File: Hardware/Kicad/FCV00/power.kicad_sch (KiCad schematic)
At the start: 52 parts, among them U1 TPS54360BDDAR, U2 TPS54360BDDAR, U3 AP2112K-3.3TRG1, U4 AP2112K-3.3TRG1

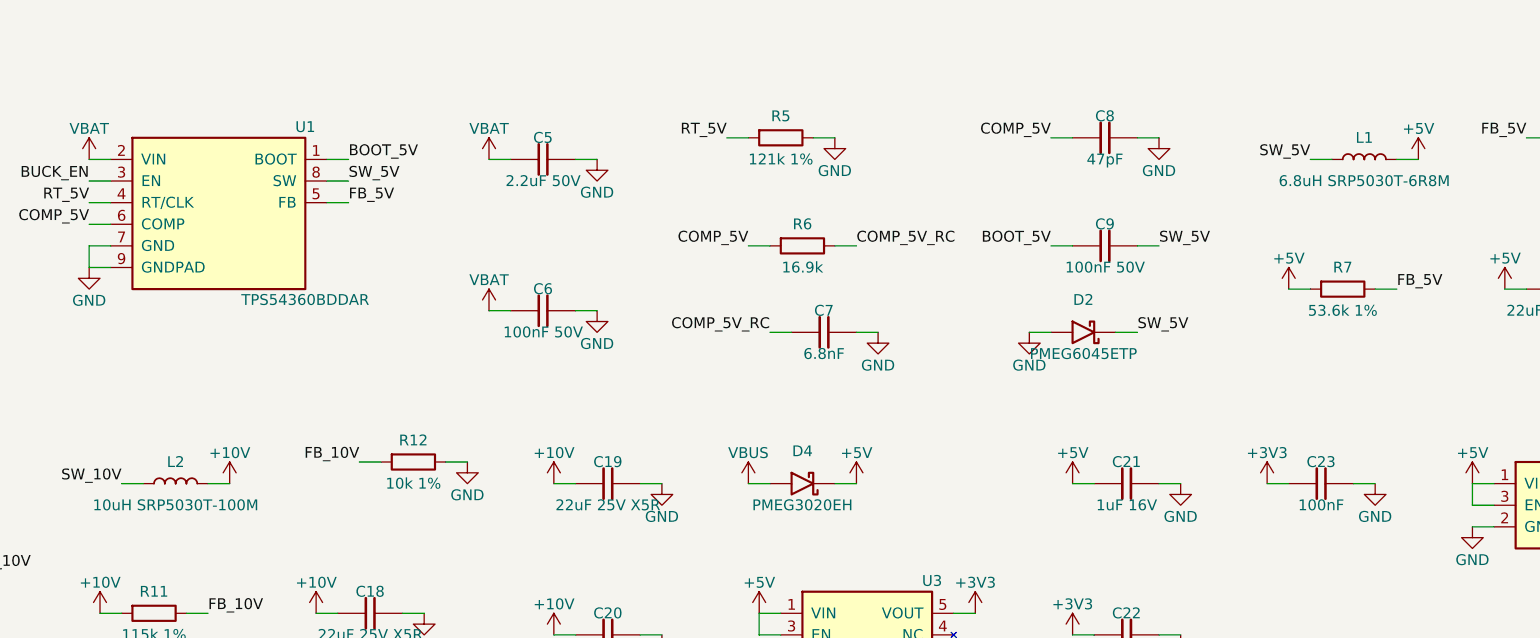
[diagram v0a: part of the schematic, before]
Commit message: Upgrade to KiCad 10 and use shared Kicad_Libs only
- Upgrade ESCV00, FCV00, RXV00, VTXV00 schematics and PCBs to KiCad 10
- Remove KiCad_Libs_Drone and merge_libs (parts already in Kicad_Libs)
- Lib tables list every Kicad_Libs library
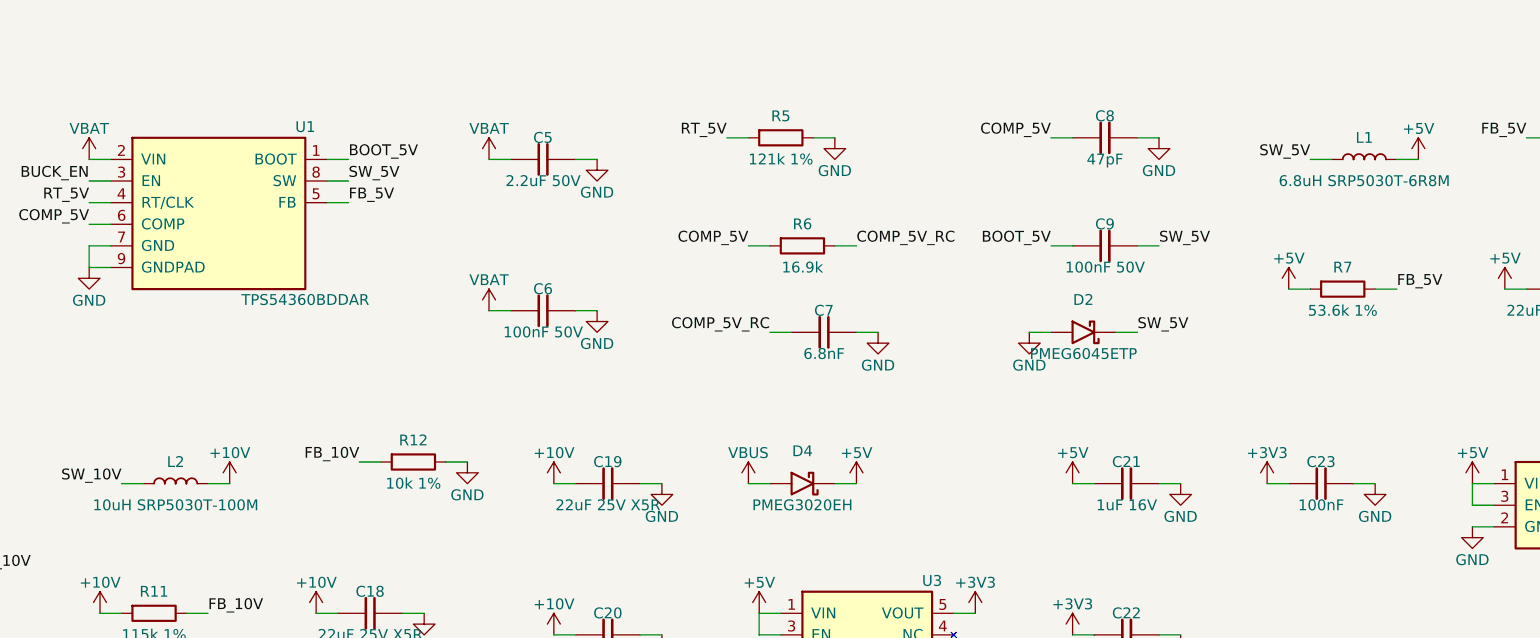
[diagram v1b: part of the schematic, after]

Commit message: Boards follow the B0_EE part convention
- every real part uses the symbol/footprint/3D/datasheet named after its MPN in Kicad_Libs
- symbols keep only Reference, Value, Footprint, Datasheet, Description
  (MPN, Manufacturer, Verify, LCSC, Note fields removed; Verify notes moved to the Readme)
- schematic symbol caches rebuilt from the libraries, PCB footprints relinked with the
  same fields and 3D models as the library (connectivity unchanged)
- DNP and BOM attributes of the footprints match the symbols
- BOMs re-exported with kicad-cli
- ignore KiCad local history
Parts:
- D1: footprint eDiodes:D_SMA -> eDiodes:SMAJ28A; symbol eDiodes:D_TVS -> eDiodes:SMAJ28A; MPN SMAJ28A -> (none)
- D2, D3: value PMEG6045ETP -> PMEG6045ETPX; footprint eDiodes:D_SOD-128 -> eDiodes:PMEG6045ETPX; symbol eDiodes:D_Schottky -> eDiodes:PMEG6045ETPX; MPN PMEG6045ETPX -> (none)
- D4: footprint eDiodes:D_SOD-123F -> eDiodes:PMEG3020EH; symbol eDiodes:D_Schottky -> eDiodes:PMEG3020EH; MPN PMEG3020EH,115 -> (none)
- D5: value RED -> KT-0603R; footprint eLED:LED_0603_1608Metric -> eLED:KT-0603R; symbol eLED:LED -> eLED:KT-0603R; MPN KT-0603R -> (none)
- L1: value 6.8uH SRP5030T-6R8M -> SRP5030T-6R8M; footprint eCoil:L_Bourns_SRP5030T -> eCoil:SRP5030T-6R8M; symbol eCoil:L -> eCoil:SRP5030T-6R8M; MPN SRP5030T-6R8M -> (none); Manufacturer Bourns -> (none)
- L2: value 10uH SRP5030T-100M -> SRP5030T-100M; footprint eCoil:L_Bourns_SRP5030T -> eCoil:SRP5030T-100M; symbol eCoil:L -> eCoil:SRP5030T-100M; MPN SRP5030T-100M -> (none); Manufacturer Bourns -> (none)
- TP1, TP2: now left out of the parts list
- U1, U2: footprint eConverterDCDC:TI_SO-PowerPAD-8_ThermalVias -> eConverterDCDC:TPS54360BDDAR; MPN TPS54360BDDAR -> (none); Manufacturer Texas Instruments -> (none)
- U3, U4: footprint eLinearReg:SOT-23-5 -> eLinearReg:AP2112K-3.3TRG1; LCSC C51118 -> (none); MPN AP2112K-3.3TRG1 -> (none); Manufacturer Diodes Inc -> (none)

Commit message: Cleared all the descriptions and started Power section for FCV
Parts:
- removed C1, C2: 10uF 50V X7R, eCapacitor:C_1206_3216Metric, symbol eCapacitor:C
- removed C10, C11: 22uF 16V X5R, eCapacitor:C_0805_2012Metric, symbol eCapacitor:C
- removed C12, C20, C23, C26, C4: 100nF, eCapacitor:C_0402_1005Metric, symbol eCapacitor:C
- removed C13, C5: 2.2uF 50V, eCapacitor:C_0805_2012Metric, symbol eCapacitor:C
- removed C14, C17, C3, C6, C9: 100nF 50V, eCapacitor:C_0603_1608Metric, symbol eCapacitor:C
- removed C15: 4.7nF, eCapacitor:C_0402_1005Metric, symbol eCapacitor:C
- removed C16: 33pF, eCapacitor:C_0402_1005Metric, symbol eCapacitor:C
- removed C18, C19: 22uF 25V X5R, eCapacitor:C_1206_3216Metric, symbol eCapacitor:C
- removed C21, C24: 1uF 16V, eCapacitor:C_0402_1005Metric, symbol eCapacitor:C
- removed C22, C25: 4.7uF 10V, eCapacitor:C_0603_1608Metric, symbol eCapacitor:C
- removed C7: 6.8nF, eCapacitor:C_0402_1005Metric, symbol eCapacitor:C
- removed C8: 47pF, eCapacitor:C_0402_1005Metric, symbol eCapacitor:C
- removed D1: SMAJ28A, eDiodes:SMAJ28A, symbol eDiodes:SMAJ28A
- removed D2, D3: PMEG6045ETPX, eDiodes:PMEG6045ETPX, symbol eDiodes:PMEG6045ETPX
- removed D4: PMEG3020EH, eDiodes:PMEG3020EH, symbol eDiodes:PMEG3020EH
- removed D5: KT-0603R, eLED:KT-0603R, symbol eLED:KT-0603R
- removed L1: SRP5030T-6R8M, eCoil:SRP5030T-6R8M, symbol eCoil:SRP5030T-6R8M
- removed L2: SRP5030T-100M, eCoil:SRP5030T-100M, symbol eCoil:SRP5030T-100M
- removed R1, R12: 10k 1%, eResistor:R_0402_1005Metric, symbol eResistor:R
- removed R10: 24.9k, eResistor:R_0402_1005Metric, symbol eResistor:R
- removed R11: 115k 1%, eResistor:R_0402_1005Metric, symbol eResistor:R
- removed R13: 1k, eResistor:R_0402_1005Metric, symbol eResistor:R
- removed R2: 1k 1%, eResistor:R_0402_1005Metric, symbol eResistor:R
- removed R3: 470k, eResistor:R_0402_1005Metric, symbol eResistor:R
- removed R4: 100k, eResistor:R_0402_1005Metric, symbol eResistor:R
- removed R5, R9: 121k 1%, eResistor:R_0402_1005Metric, symbol eResistor:R
- removed R6: 16.9k, eResistor:R_0402_1005Metric, symbol eResistor:R
- removed R7: 53.6k 1%, eResistor:R_0402_1005Metric, symbol eResistor:R
- removed R8: 10.2k 1%, eResistor:R_0402_1005Metric, symbol eResistor:R
- removed TP1: BAT+, eConnector:SolderPad_3x5mm, symbol eTestPoint:TestPoint
- removed TP2: BAT-, eConnector:SolderPad_3x5mm, symbol eTestPoint:TestPoint
- removed U2: TPS54360BDDAR, eConverterDCDC:TPS54360BDDAR, symbol eConverterDCDC:TPS54360BDDAR
- removed U3: AP2112K-3.3TRG1, eLinearReg:AP2112K-3.3TRG1, symbol eLinearReg:AP2112K-3.3TRG1
- added C10, C16, C17, C9: 2u2, symbol Device:C
- added C11, C18: 100n, symbol Device:C
- added C12, C13, C21, C22: 47u, symbol Device:C
- added C14: 6800p, symbol Device:C
- added C15: 39p, symbol Device:C
- added C19: 8n2, symbol Device:C
- added C20: 33p, symbol Device:C
- added C23, C24, C25, C26: 1u, symbol Device:C
- added D2, D3: B560C, symbol eDiodes:D_Schottky
- added L2: 8u2, symbol Device:L
- added L3: 15u, symbol Device:L
- added R10, R37: 10k2, symbol Device:R
- added R11: 294k, symbol Device:R
- added R12: 31k6, symbol Device:R
- added R13, R7: 162k, symbol Device:R
- added R35: 15k, symbol Device:R
- added R36: 118k, symbol Device:R
- added R5: 523k, symbol Device:R
- added R6: 84k5, symbol Device:R
- added R8: 13k, symbol Device:R
- added R9: 53k6, symbol Device:R
- added U10: TPS54360BDDAR, eConverterDCDC:TPS54360BDDAR, symbol eConverterDCDC:TPS54360BDDAR
- added U11: AP2112K-3.3TRG1, eLinearReg:AP2112K-3.3TRG1, symbol eLinearReg:AP2112K-3.3TRG1
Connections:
- net +3V3: now also C26.2, U11.5 (VOUT)
- net +3V3_GYRO: now also C24.2
- net +5V: now also C23.2, C25.2, U11.1 (VIN), U11.3 (EN)
- net GND: now also C10.2, C12.1, C13.1, C14.1, C15.1, C16.2, C17.2, C19.1, C20.1, C21.1, C22.1, C23.1, C24.1, C25.1, C26.1, C9.2, D2.2 (A), D3.2 (A), R10.2, R12.2, R13.2, R37.2, R6.2, R7.2, U10.7 (GND), U10.9 (GNDPAD), U11.2 (GND)
- net VBAT: now also C10.1, C16.1, C17.1, C9.1, R11.1, R5.1, U10.2 (VIN)
- net BOOT_5V: no longer names the net of U1.1 (BOOT)
- net BOOT_5V: now also C11.1
- net BUCK_EN: no longer names the net of U1.3 (EN)
- net BUCK_EN: now also R5.2, R6.1
- net COMP_5V: no longer names the net of U1.6 (COMP)
- net COMP_5V: now also C15.2, R8.1
- net FB_5V: no longer names the net of U1.5 (FB)
- net FB_5V: now also R10.1, R9.2
- net RT_5V: no longer names the net of U1.4 (RT/CLK)
- net RT_5V: now also R7.1
- net SW_5V: no longer names the net of U1.8 (SW)
- net SW_5V: now also C11.2, D2.1 (K), L2.1
- new net: C18.1, U10.1 (BOOT)
- new net: R11.2, R12.1, U10.3 (EN)
- new net: R13.1, U10.4 (RT/CLK)
- new net: R36.2, R37.1, U10.5 (FB)
- new net: C20.2, R35.1, U10.6 (COMP)
- new net: C18.2, D3.1 (K), L3.1, U10.8 (SW)
- new net: C19.2, R35.2
- new net: C14.2, R8.2
- new net 10V: C21.2, C22.2, L3.2, R36.1
- new net 5V: C12.2, C13.2, L2.2, R9.1
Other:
- note added: "12 to 60V"
- note added: "5V -> 3V3"
- note added: "5V -> 3V3 GYRO"
- note added: "VBAT -> 10V"
- note added: "VBAT -> 5V"
- note added: "per i 10V mi serve almeno un 4S , con 3S rischio di arrivare a 9.9V Quindi pensare a cosa vogliamo fare"
- moved on the sheet: U1, U4
